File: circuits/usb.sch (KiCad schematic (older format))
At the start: 15 parts, among them J11 USB_MINI_B, J12 Conn_02x02_Counter_Clockwise, Q17 Q_NPN, Q18 Q_PNP, U16 FT231XS

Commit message: Sent to fab.
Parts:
- removed C27, C28: C_47pF, Capacitor_SMD:C_0603_1608Metric_Pad1.08x0.95mm_HandSolder, symbol Open_Automation:C_47pF
- removed C29, C31: C_0.1uF, Capacitor_SMD:C_0603_1608Metric_Pad1.08x0.95mm_HandSolder, symbol Open_Automation:C_0.1uF
- removed C30: C_4.7uF, Capacitor_SMD:C_0603_1608Metric_Pad1.08x0.95mm_HandSolder, symbol Open_Automation:C_4.7uF
- removed D14: D_1N5819HW, Diode_SMD:D_SOD-123, symbol Open_Automation:D_1N5819HW
- removed J12: Conn_02x02_Counter_Clockwise, Connector_PinHeader_2.54mm:PinHeader_2x02_P2.54mm_Vertical, symbol Connector_Generic:Conn_02x02_Counter_Clockwise
- removed Q17: Q_NPN, Package_TO_SOT_SMD:SOT-23, symbol Open_Automation:Q_NPN
- removed Q18: Q_PNP, Package_TO_SOT_SMD:SOT-23, symbol Open_Automation:Q_PNP
- removed R84, R85: R_27, Resistor_SMD:R_0603_1608Metric_Pad0.98x0.95mm_HandSolder, symbol Open_Automation:R_27
- removed R86, R87: R_10K, Resistor_SMD:R_0603_1608Metric_Pad0.98x0.95mm_HandSolder, symbol Open_Automation:R_10K
- removed U16: FT231XS, Package_SO:SSOP-20_3.9x8.7mm_P0.635mm, symbol Open_Automation:FT231XS
- added C10: C_100nF_0402, Capacitor_SMD:C_0402_1005Metric_Pad0.74x0.62mm_HandSolder, symbol Open_Automation:C_100nF_0402
- added C7, C8: C_27pF_0402, Capacitor_SMD:C_0402_1005Metric_Pad0.74x0.62mm_HandSolder, symbol Open_Automation:C_27pF_0402
- added C9: C_22uF, Capacitor_SMD:C_0603_1608Metric_Pad1.08x0.95mm_HandSolder, symbol Open_Automation:C_22uF
- added D4, D5: D_1N5819, Diode_SMD:D_SOD-323_HandSoldering, symbol Open_Automation:D_1N5819
- added D6: BAT54C, Package_TO_SOT_SMD:SOT-23, symbol Open_Automation:BAT54C
- added Q5: Crystal_12Mhz, Crystal:Crystal_SMD_3225-4Pin_3.2x2.5mm_HandSoldering, symbol Open_Automation:Crystal_12Mhz
- added Q6: Q_SS8050, Package_TO_SOT_SMD:SOT-23, symbol Open_Automation:Q_SS8050
- added Q7: Q_SS8550, Package_TO_SOT_SMD:SOT-23, symbol Open_Automation:Q_SS8550
- added R40, R41, R45: R_10K_0402, Resistor_SMD:R_0402_1005Metric_Pad0.72x0.64mm_HandSolder, symbol Open_Automation:R_10K_0402
- added R42, R43: R_1K_0402, Resistor_SMD:R_0402_1005Metric_Pad0.72x0.64mm_HandSolder, symbol Open_Automation:R_1K_0402
- added R44: R_220_0402, Resistor_SMD:R_0402_1005Metric_Pad0.72x0.64mm_HandSolder, symbol Open_Automation:R_220_0402
- added U10: CH340T(SSOP20W), Open_Automation:SSOP-20W, symbol Open_Automation:CH340T(SSOP20W)
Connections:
- net labels added: +3.3V, +5V_USB, 3V3, D+, D-, D_Com, GPIO0, GPIO1\U0TXD, GPIO2\HS2_DATA0, GPIO3\U0RXD, IO2
- net labels removed: 3V3OUT, DCD, DSR, DTR, RTS, USBDM, USBDP, VBUS, VSENSE
- wire segments 48 -> 74
- no-connect marks 0 -> 6
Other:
- note added: "!!!WARNING!!!\nWhen the board is powered via PoE, don't include the USB cable for to programming it!!!\nIn case this is required, USB-ISO must be used for to guarantee galvanic isolation!\nSee: https://www.olimex.com/Products/USB-Modules/USB-ISO/"
- note added: "0"
- note added: "1"
- note added: "Auto program\n"
- note added: "DTR RTS->EN IO0"

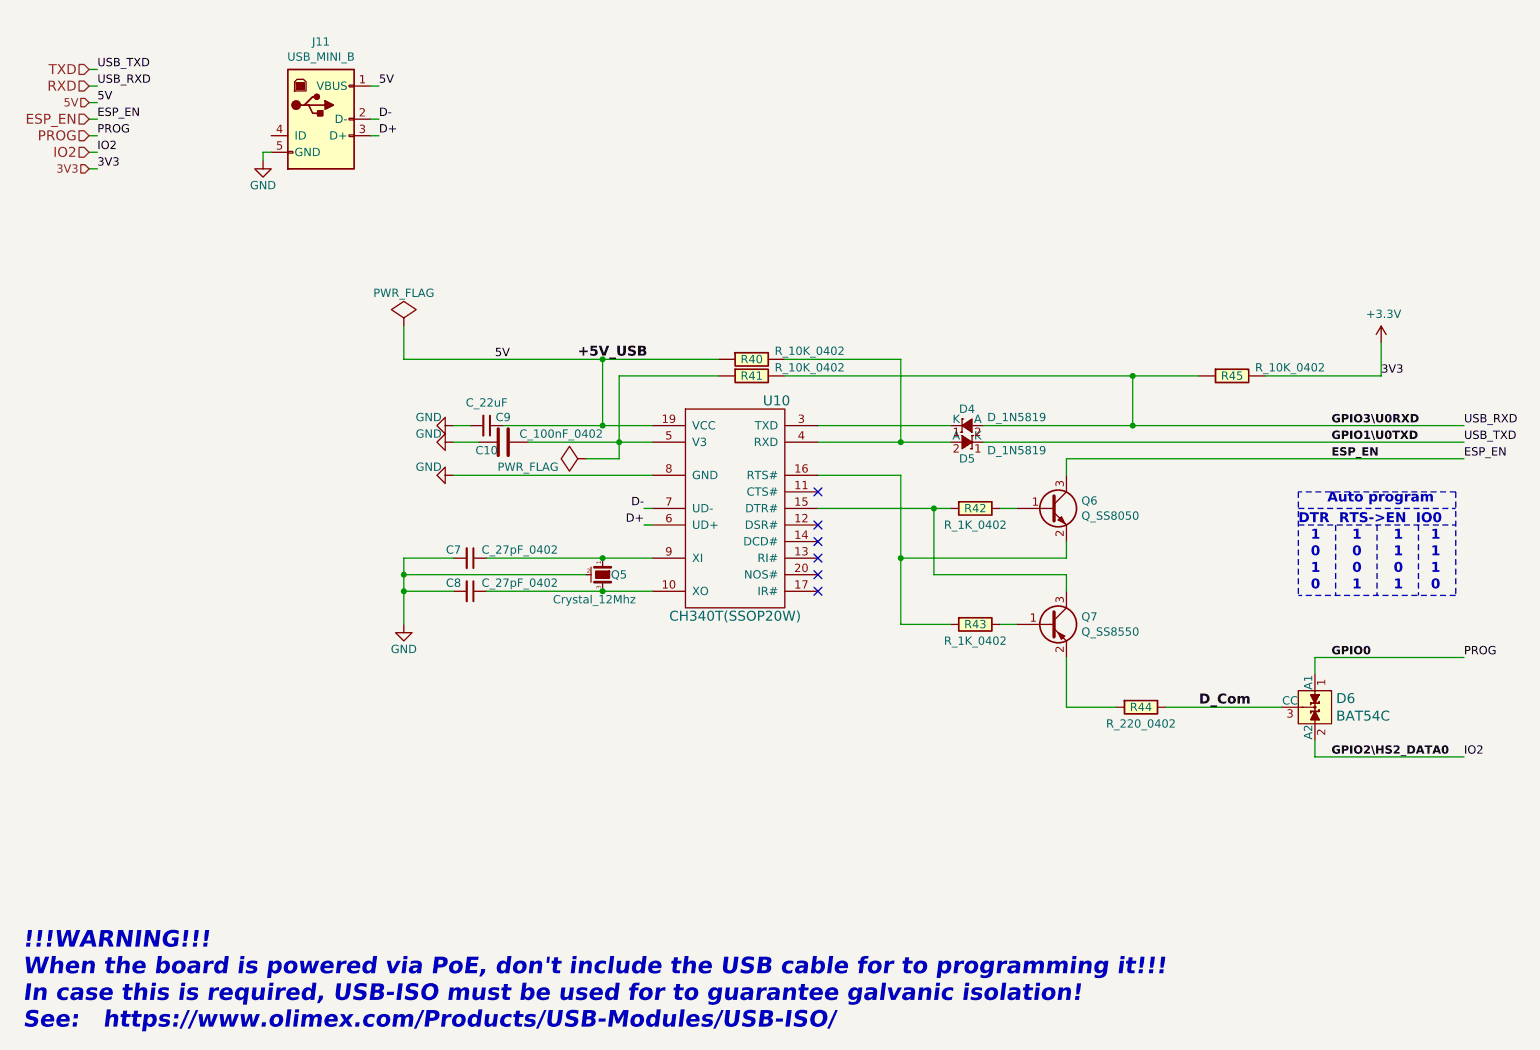
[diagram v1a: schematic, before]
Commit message: finished schematic corrections, working on layout
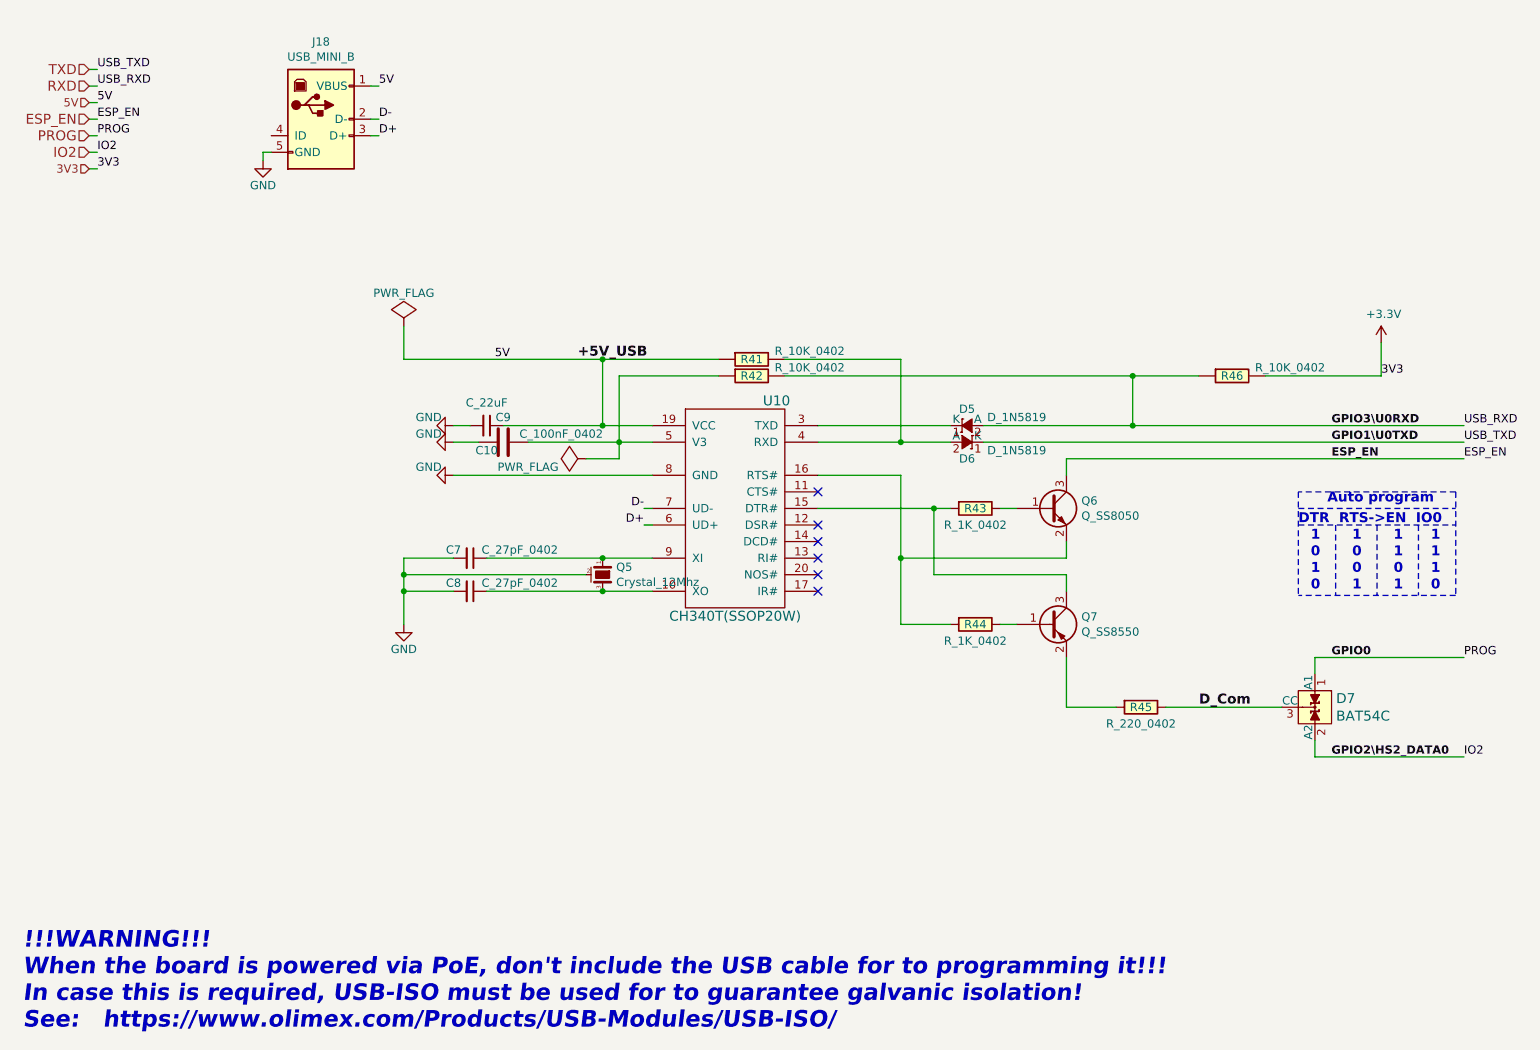
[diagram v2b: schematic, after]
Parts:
- renumbered D4 to D5, D5 to D6, D6 to D7, J11 to J18, R40 to R41, R41 to R42, R42 to R43, R43 to R44, R44 to R45, R45 to R46
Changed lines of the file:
@@
 3V3
 $Comp
-L ESP32-PoE_Rev_E:+3.3V #PWR083
+L ESP32-PoE_Rev_E:+3.3V #PWR080
 U 1 1 60036A30
 P 8750 2500
-F 0 "#PWR083" H 8750 2350 50  0001 C CNN
+F 0 "#PWR080" H 8750 2350 50  0001 C CNN
 F 1 "+3.3V" H 8765 2673 50  0000 C CNN
 F 2 "" H 8750 2500 60  0000 C CNN
@@
 IO2
 $Comp
-L Open_Automation:USB_MINI_B J11
+L Open_Automation:USB_MINI_B J18
 U 1 1 603DE312
 P 2350 1150
-F 0 "J11" H 2350 1617 50  0000 C CNN
+F 0 "J18" H 2350 1617 50  0000 C CNN
 F 1 "USB_MINI_B" H 2350 1526 50  0000 C CNN
 F 2 "Open_Automation:USB-mini-B-0548190519" H 2250 1900 50  0001 C CNN
@@
 AR Path="/604145B1" Ref="#PWR?"  Part="1"
 AR Path="/5A7BADB8/604145B1" Ref="#PWR?"  Part="1"
-AR Path="/60DDD162/604145B1" Ref="#PWR079"  Part="1"
-F 0 "#PWR079" H 2850 3950 50  0001 C CNN
+AR Path="/60DDD162/604145B1" Ref="#PWR076"  Part="1"
+F 0 "#PWR076" H 2850 3950 50  0001 C CNN
 F 1 "GND" H 2850 4050 50  0000 C CNN
 F 2 "" H 2850 4200 50  0001 C CNN
@@
 AR Path="/6041598A" Ref="#PWR?"  Part="1"
 AR Path="/5A7BADB8/6041598A" Ref="#PWR?"  Part="1"
-AR Path="/60DDD162/6041598A" Ref="#PWR078"  Part="1"
-F 0 "#PWR078" H 2000 1150 50  0001 C CNN
+AR Path="/60DDD162/6041598A" Ref="#PWR075"  Part="1"
+F 0 "#PWR075" H 2000 1150 50  0001 C CNN
 F 1 "GND" H 2000 1250 50  0000 C CNN
 F 2 "" H 2000 1400 50  0001 C CNN
@@
 AR Path="/6042DDD6" Ref="#PWR?"  Part="1"
 AR Path="/5A7BADB8/6042DDD6" Ref="#PWR?"  Part="1"
-AR Path="/60DDD162/6042DDD6" Ref="#PWR080"  Part="1"
-F 0 "#PWR080" H 3150 2750 50  0001 C CNN
+AR Path="/60DDD162/6042DDD6" Ref="#PWR077"  Part="1"
+F 0 "#PWR077" H 3150 2750 50  0001 C CNN
 F 1 "GND" V 3100 2850 50  0000 C CNN
 F 2 "" H 3150 3000 50  0001 C CNN
@@
 AR Path="/6042E609" Ref="#PWR?"  Part="1"
 AR Path="/5A7BADB8/6042E609" Ref="#PWR?"  Part="1"
-AR Path="/60DDD162/6042E609" Ref="#PWR081"  Part="1"
-F 0 "#PWR081" H 3150 2850 50  0001 C CNN
+AR Path="/60DDD162/6042E609" Ref="#PWR078"  Part="1"
+F 0 "#PWR078" H 3150 2850 50  0001 C CNN
 F 1 "GND" V 3100 2950 50  0000 C CNN
 F 2 "" H 3150 3100 50  0001 C CNN
@@
 AR Path="/6042E874" Ref="#PWR?"  Part="1"
 AR Path="/5A7BADB8/6042E874" Ref="#PWR?"  Part="1"
-AR Path="/60DDD162/6042E874" Ref="#PWR082"  Part="1"
-F 0 "#PWR082" H 3150 3050 50  0001 C CNN
+AR Path="/60DDD162/6042E874" Ref="#PWR079"  Part="1"
+F 0 "#PWR079" H 3150 3050 50  0001 C CNN
 F 1 "GND" V 3100 3150 50  0000 C CNN
 F 2 "" H 3150 3300 50  0001 C CNN
@@
 $EndComp
 $Comp
-L Open_Automation:R_10K_0402 R40
+L Open_Automation:R_10K_0402 R41
 U 1 1 6043D0F4
 P 4950 2600
-F 0 "R40" V 4950 2600 50  0000 C CNN
+F 0 "R41" V 4950 2600 50  0000 C CNN
 F 1 "R_10K_0402" V 4900 2950 50  0000 C CNN
 F 2 "Resistor_SMD:R_0402_1005Metric_Pad0.72x0.64mm_HandSolder" V 4880 2600 50  0001 C CNN
@@
 $EndComp
 $Comp
-L Open_Automation:R_10K_0402 R41
+L Open_Automation:R_10K_0402 R42
 U 1 1 60446CBF
 P 4950 2700
-F 0 "R41" V 4950 2700 50  0000 C CNN
+F 0 "R42" V 4950 2700 50  0000 C CNN
 F 1 "R_10K_0402" V 4900 3050 50  0000 C CNN
 F 2 "Resistor_SMD:R_0402_1005Metric_Pad0.72x0.64mm_HandSolder" V 4880 2700 50  0001 C CNN
@@
 $EndComp
 $Comp
-L Open_Automation:Crystal_12Mhz Q5
-U 1 1 6045824B
-P 4050 3900
-F 0 "Q5" V 4050 3950 50  0000 L CNN
-F 1 "Crystal_12Mhz" V 4200 3600 50  0000 L CNN
-F 2 "Crystal:Crystal_SMD_3225-4Pin_3.2x2.5mm_HandSoldering" H 4050 3900 60  0001 C CNN
-F 3 "https://datasheet.lcsc.com/szlcsc/Yangxing-Tech-X322512MSB4SI_C9002.pdf" H 4050 3900 60  0001 C CNN
-F 4 "X322512MSB4SI" H 4050 3900 50  0001 C CNN "Part Number"
-F 5 "C9002" H 4050 3900 50  0001 C CNN "LCSC"
-	1    4050 3900
-	0    1    1    0
-$EndComp
-Wire Wire Line
-	3350 3800 4050 3800
-Wire Wire Line
-	3350 4000 4050 4000
-Connection ~ 4050 3800
-Wire Wire Line
-	4050 3800 4350 3800
-Connection ~ 4050 4000
-Wire Wire Line
-	4050 4000 4350 4000
-$Comp
-L Open_Automation:R_10K_0402 R45
+L Open_Automation:R_10K_0402 R46
 U 1 1 6045B2FE
 P 7850 2700
-F 0 "R45" V 7850 2700 50  0000 C CNN
+F 0 "R46" V 7850 2700 50  0000 C CNN
 F 1 "R_10K_0402" V 7800 3050 50  0000 C CNN
 F 2 "Resistor_SMD:R_0402_1005Metric_Pad0.72x0.64mm_HandSolder" V 7780 2700 50  0001 C CNN
@@
 Connection ~ 7250 2700
 $Comp
-L Open_Automation:R_1K_0402 R43
+L Open_Automation:R_1K_0402 R44
 U 1 1 6045ED26
 P 6300 4200
-F 0 "R43" V 6300 4200 50  0000 C CNN
+F 0 "R44" V 6300 4200 50  0000 C CNN
 F 1 "R_1K_0402" V 6400 4200 50  0000 C CNN
 F 2 "Resistor_SMD:R_0402_1005Metric_Pad0.72x0.64mm_HandSolder" V 6230 4200 50  0001 C CNN
@@
 $EndComp
 $Comp
-L Open_Automation:R_1K_0402 R42
+L Open_Automation:R_1K_0402 R43
 U 1 1 60460EF6
 P 6300 3500
-F 0 "R42" V 6300 3500 50  0000 C CNN
+F 0 "R43" V 6300 3500 50  0000 C CNN
 F 1 "R_1K_0402" V 6400 3500 50  0000 C CNN
 F 2 "Resistor_SMD:R_0402_1005Metric_Pad0.72x0.64mm_HandSolder" V 6230 3500 50  0001 C CNN
@@
 $EndComp
 $Comp
-L Open_Automation:D_1N5819 D4
+L Open_Automation:D_1N5819 D5
 U 1 1 6046A572
 P 6250 3000
-F 0 "D4" H 6250 3100 50  0000 C CNN
+F 0 "D5" H 6250 3100 50  0000 C CNN
 F 1 "D_1N5819" H 6550 3050 50  0000 C CNN
 F 2 "Diode_SMD:D_SOD-323_HandSoldering" V 6250 3000 60  0001 C CNN
@@
 $EndComp
 $Comp
-L Open_Automation:D_1N5819 D5
+L Open_Automation:D_1N5819 D6
 U 1 1 6046B2F8
 P 6250 3100
-F 0 "D5" H 6250 3200 50  0000 C CNN
+F 0 "D6" H 6250 3200 50  0000 C CNN
 F 1 "D_1N5819" H 5950 3150 50  0000 C CNN
 F 2 "Diode_SMD:D_SOD-323_HandSoldering" V 6250 3100 60  0001 C CNN
@@
 $EndComp
 $Comp
-L Open_Automation:R_220_0402 R44
+L Open_Automation:R_220_0402 R45
 U 1 1 604ACCCE
 P 7300 4700
-F 0 "R44" V 7300 4700 50  0000 C CNN
+F 0 "R45" V 7300 4700 50  0000 C CNN
 F 1 "R_220_0402" V 7400 4700 50  0000 C CNN
 F 2 "Resistor_SMD:R_0402_1005Metric_Pad0.72x0.64mm_HandSolder" V 7230 4700 50  0001 C CNN
@@
 $EndComp
 $Comp
-L Open_Automation:BAT54C D6
+L Open_Automation:BAT54C D7
 U 1 1 604B459D
 P 8350 4700
-F 0 "D6" V 8297 4828 60  0000 L CNN
+F 0 "D7" V 8297 4828 60  0000 L CNN
 F 1 "BAT54C" V 8403 4828 60  0000 L CNN
 F 2 "Package_TO_SOT_SMD:SOT-23" H 8350 4700 60  0001 C CNN
@@
 	1    0    0    -1
 $EndComp
+$Comp
+L Open_Automation:Crystal_12Mhz Q5
+U 1 1 613C96CC
+P 4050 3900
+F 0 "Q5" V 4004 3982 50  0000 L CNN
+F 1 "Crystal_12Mhz" V 4095 3982 50  0000 L CNN
+F 2 "Crystal:Crystal_SMD_3225-4Pin_3.2x2.5mm_HandSoldering" H 4050 4200 60  0001 C CNN
+F 3 "https://datasheet.lcsc.com/szlcsc/Yangxing-Tech-X322512MSB4SI_C9002.pdf" H 4050 3900 60  0001 C CNN
+F 4 "X322512MSB4SI" H 4050 4100 50  0001 C CNN "Part Number"
+F 5 "C9002" H 4050 4300 50  0001 C CNN "LCSC"
+	1    4050 3900
+	0    1    1    0
+$EndComp
+Wire Wire Line
+	3350 3800 4050 3800
+Wire Wire Line
+	3350 4000 4050 4000
+Connection ~ 4050 3800
+Wire Wire Line
+	4050 3800 4350 3800
+Connection ~ 4050 4000
+Wire Wire Line
+	4050 4000 4350 4000
 $EndSCHEMATC

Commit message: finished layout, sent to board house
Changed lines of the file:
@@
 	1    0    0    -1
 $EndComp
+Wire Wire Line
+	4050 4000 4350 4000
+Wire Wire Line
+	3350 4000 4050 4000
+Connection ~ 4050 4000
+Wire Wire Line
+	4050 3800 4350 3800
+Wire Wire Line
+	3350 3800 4050 3800
+Connection ~ 4050 3800
 $Comp
 L Open_Automation:Crystal_12Mhz Q5
-U 1 1 613C96CC
+U 1 1 6045824B
 P 4050 3900
-F 0 "Q5" V 4004 3982 50  0000 L CNN
-F 1 "Crystal_12Mhz" V 4095 3982 50  0000 L CNN
-F 2 "Crystal:Crystal_SMD_3225-4Pin_3.2x2.5mm_HandSoldering" H 4050 4200 60  0001 C CNN
+F 0 "Q5" V 4050 3950 50  0000 L CNN
+F 1 "Crystal_12Mhz" V 4200 3600 50  0000 L CNN
+F 2 "Crystal:Crystal_SMD_3225-4Pin_3.2x2.5mm_HandSoldering" H 4050 3900 60  0001 C CNN
 F 3 "https://datasheet.lcsc.com/szlcsc/Yangxing-Tech-X322512MSB4SI_C9002.pdf" H 4050 3900 60  0001 C CNN
-F 4 "X322512MSB4SI" H 4050 4100 50  0001 C CNN "Part Number"
-F 5 "C9002" H 4050 4300 50  0001 C CNN "LCSC"
+F 4 "X322512MSB4SI" H 4050 3900 50  0001 C CNN "Part Number"
+F 5 "C9002" H 4050 3900 50  0001 C CNN "LCSC"
 	1    4050 3900
 	0    1    1    0
 $EndComp
-Wire Wire Line
-	3350 3800 4050 3800
-Wire Wire Line
-	3350 4000 4050 4000
-Connection ~ 4050 3800
-Wire Wire Line
-	4050 3800 4350 3800
-Connection ~ 4050 4000
-Wire Wire Line
-	4050 4000 4350 4000
 $EndSCHEMATC

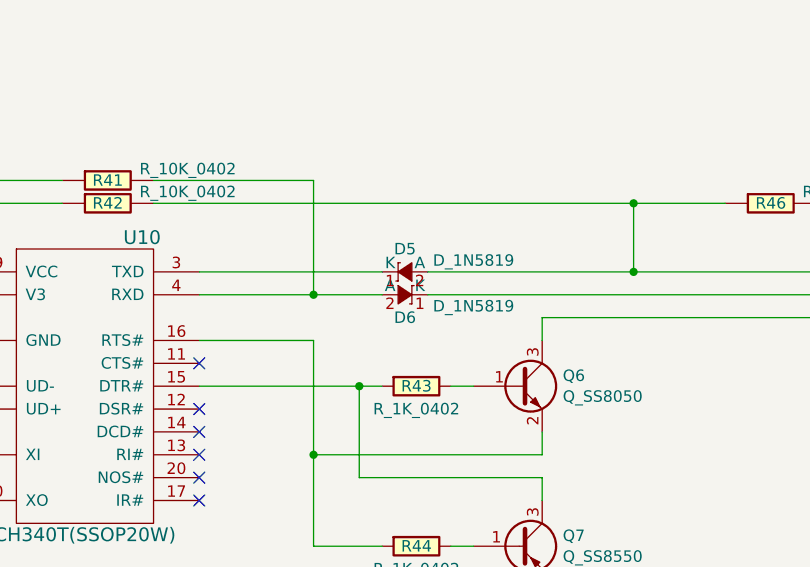
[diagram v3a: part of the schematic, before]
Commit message: Disable Keypad when fob disarms lock. This is so the keypad does not rearm the lock if used.
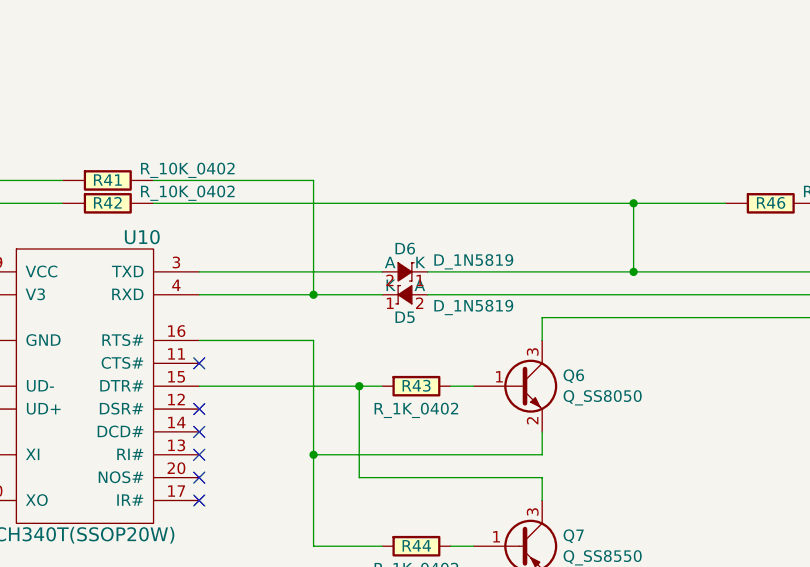
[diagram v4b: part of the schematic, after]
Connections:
- net RXD: now also D5.1 (K); no longer D5.2 (A)
- net TXD: now also D6.2 (A); no longer D6.1 (K)
- net at R41.2, U10.4 (RXD): now also D6.1 (K); no longer D6.2 (A)
- net at U10.3 (TXD): now also D5.2 (A); no longer D5.1 (K)
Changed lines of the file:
@@
 U 1 1 6046A572
 P 6250 3000
-F 0 "D5" H 6250 3100 50  0000 C CNN
-F 1 "D_1N5819" H 6550 3050 50  0000 C CNN
+F 0 "D5" H 6250 3200 50  0000 C CNN
+F 1 "D_1N5819" H 5950 2950 50  0000 C CNN
 F 2 "Diode_SMD:D_SOD-323_HandSoldering" V 6250 3000 60  0001 C CNN
 F 3 "https://datasheet.lcsc.com/szlcsc/1903051130_MDD-Jiangsu-Yutai-Elec-B5819WS_C64886.pdf" V 6250 3000 60  0001 C CNN
@@
 F 5 "C64886" H 6250 3000 50  0001 C CNN "LCSC"
 	1    6250 3000
-	1    0    0    -1
+	-1   0    0    1
 $EndComp
 $Comp
@@
 U 1 1 6046B2F8
 P 6250 3100
-F 0 "D6" H 6250 3200 50  0000 C CNN
-F 1 "D_1N5819" H 5950 3150 50  0000 C CNN
+F 0 "D6" H 6250 3300 50  0000 C CNN
+F 1 "D_1N5819" H 6550 3050 50  0000 C CNN
 F 2 "Diode_SMD:D_SOD-323_HandSoldering" V 6250 3100 60  0001 C CNN
 F 3 "https://datasheet.lcsc.com/szlcsc/1903051130_MDD-Jiangsu-Yutai-Elec-B5819WS_C64886.pdf" V 6250 3100 60  0001 C CNN
@@
 F 5 "C64886" H 6250 3100 50  0001 C CNN "LCSC"
 	1    6250 3100
-	-1   0    0    1
+	1    0    0    -1
 $EndComp
 $Comp
